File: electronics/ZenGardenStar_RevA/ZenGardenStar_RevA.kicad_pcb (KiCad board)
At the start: 2 copper layers, 13 parts, among them P1 CONN_01X02, P2 CONN_01X02, U1 A6211, U2 LM317_SOT223, U3 ArduinoProMini328, U4 MCP1700, U5 NRF24L01+

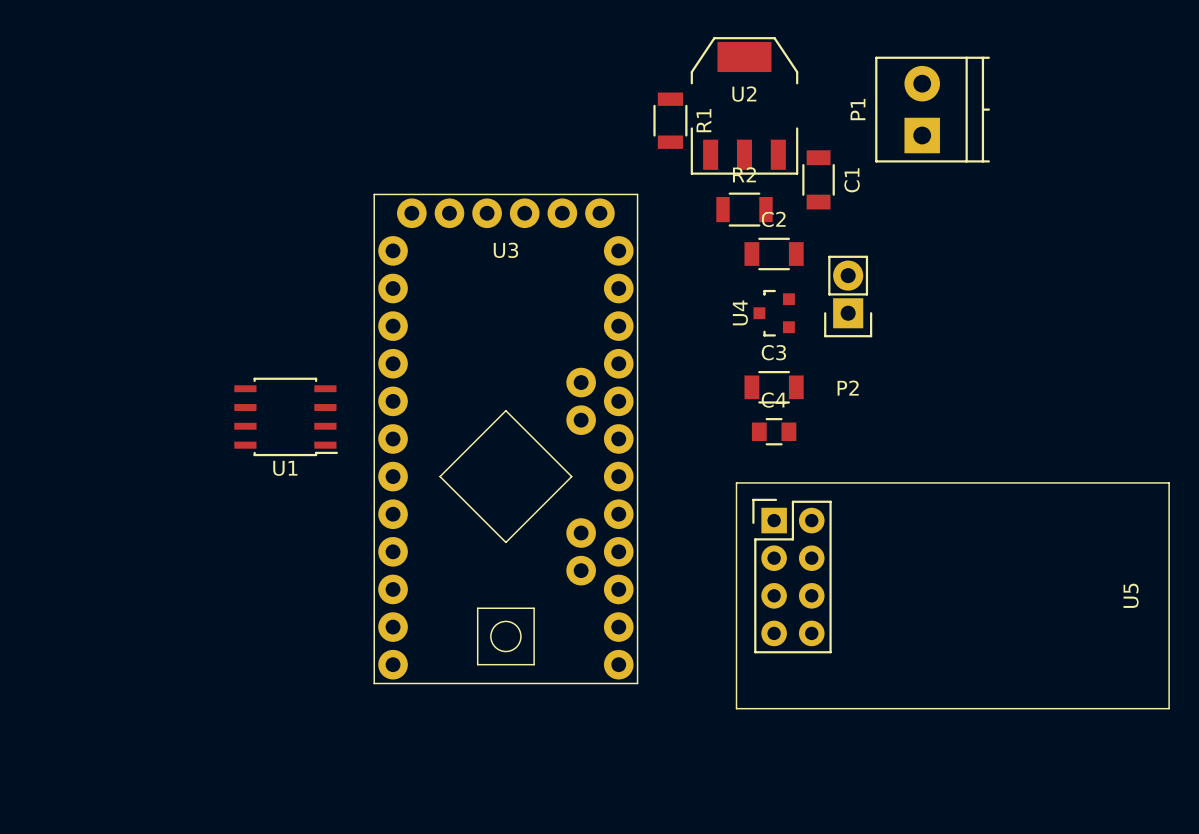
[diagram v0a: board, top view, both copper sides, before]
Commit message: updated schematic for star
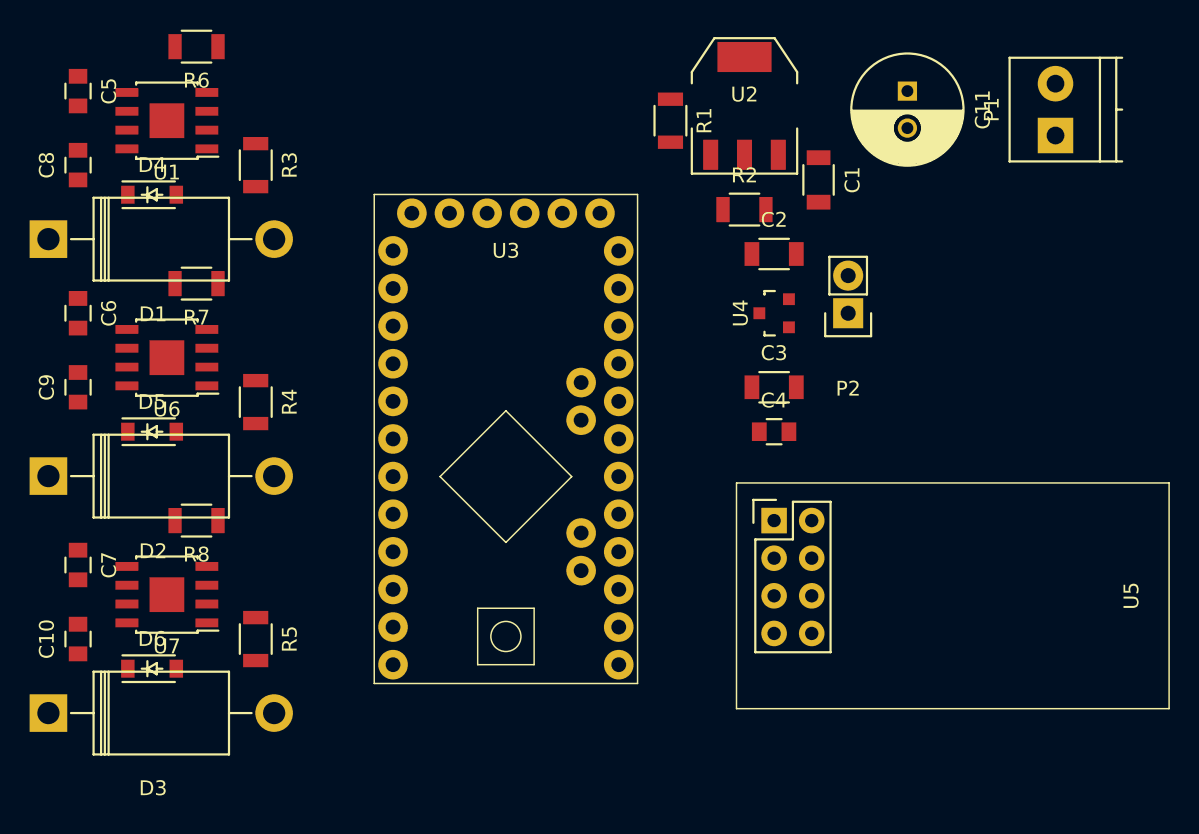
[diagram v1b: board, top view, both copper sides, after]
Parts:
- added C10: 0.047uF 50V, Capacitors_SMD:C_0805, F.Cu at (113.0, 108.0)
- added C11: 47uF 50V, Capacitors_ThroughHole:C_Radial_D7.5_L11.2_P2.5, F.Cu at (169.0, 71.0)
- added C5: 0.1uF 10V, Capacitors_SMD:C_0805, F.Cu at (113.0, 71.0)
- added C6: 0.1uF 10V, Capacitors_SMD:C_0805, F.Cu at (113.0, 86.0)
- added C7: 0.1uF 10V, Capacitors_SMD:C_0805, F.Cu at (113.0, 103.0)
- added C8: 0.047uF 50V, Capacitors_SMD:C_0805, F.Cu at (113.0, 76.0)
- added C9: 0.047uF 50V, Capacitors_SMD:C_0805, F.Cu at (113.0, 91.0)
- added D1: 60V 3A SR306, Diodes_ThroughHole:Diode_DO-201AD_Horizontal_RM15, F.Cu at (111.0, 81.0)
- added D2: 60V 3A SR306, Diodes_ThroughHole:Diode_DO-201AD_Horizontal_RM15, F.Cu at (111.0, 97.0)
- added D3: 60V 3A SR306, Diodes_ThroughHole:Diode_DO-201AD_Horizontal_RM15, F.Cu at (111.0, 113.0)
- added D4: 60V 3A PMEG6030EP, Diodes_SMD:SOD-123, F.Cu at (118.0, 78.0)
- added D5: 60V 3A PMEG6030EP, Diodes_SMD:SOD-123, F.Cu at (118.0, 94.0)
- added D6: 60V 3A PMEG6030EP, Diodes_SMD:SOD-123, F.Cu at (118.0, 110.0)
- added R3: 72K, Resistors_SMD:R_1206, F.Cu at (125.0, 76.0)
- added R4: 72K, Resistors_SMD:R_1206, F.Cu at (125.0, 92.0)
- added R5: 72K, Resistors_SMD:R_1206, F.Cu at (125.0, 108.0)
- added R6: 0.43, Resistors_SMD:R_1206, F.Cu at (121.0, 68.0)
- added R7: 0.43, Resistors_SMD:R_1206, F.Cu at (121.0, 84.0)
- added R8: 0.43, Resistors_SMD:R_1206, F.Cu at (121.0, 100.0)
- added U6: A6211, Housings_SOIC:SOIC-8-1EP_3.9x4.9mm_Pitch1.27mm, F.Cu at (119.0, 89.0)
- added U7: A6211, Housings_SOIC:SOIC-8-1EP_3.9x4.9mm_Pitch1.27mm, F.Cu at (119.0, 105.0)
- C1: value 10uF -> 10uF 50V
- C2: value 10uF -> 10uF 10V
- U1: footprint MyKiCadParts:SOIC-8-N-80 -> Housings_SOIC:SOIC-8-1EP_3.9x4.9mm_Pitch1.27mm
- moved U1 21.5 mm to (119.0, 73.0)
- moved P1 9.00 mm to (179.0, 74.0)
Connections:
- U1 pad 2: (no net) -> Net-(R3-Pad1)
- U1 pad 4: (no net) -> Net-(R6-Pad1)
- U1 pad 5: V50 -> Net-(C5-Pad1)
- U1 pad 7: (no net) -> Net-(C8-Pad2)
- U1 pad 8: (no net) -> Net-(C8-Pad1)
- U3 pad 8: (no net) -> PWM_G
- U3 pad 9: (no net) -> PWM_B

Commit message: updated star layout and schematic and render, at 80-90% done
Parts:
- added L1: INDUCTOR_SMALL, Inductors:SELF-WE-PD-XXL, F.Cu at (104.0, 73.0)
- added L2: INDUCTOR_SMALL, Inductors:SELF-WE-PD-XXL, F.Cu at (104.0, 89.0)
- added L3: INDUCTOR_SMALL, Inductors:SELF-WE-PD-XXL, F.Cu at (104.0, 105.0)
- added P3: CONN_PIR_0, Pin_Headers:Pin_Header_Straight_1x03, F.Cu at (135.0, 110.0)
- added P4: CONN_PIR_1, Pin_Headers:Pin_Header_Straight_1x03, F.Cu at (142.0, 110.0)
- added P5: CONN_R, Pin_Headers:Pin_Header_Straight_1x02, F.Cu at (105.0, 65.0)
- added P6: CONN_B, Pin_Headers:Pin_Header_Straight_1x02, F.Cu at (105.0, 97.0)
- added P7: CONN_G, Pin_Headers:Pin_Header_Straight_1x02, F.Cu at (105.0, 81.0)
- P2: value CONN_01X02 -> CONN_VDD
- moved C11 17.5 mm to (152.0, 67.0)
- moved P1 16.8 mm to (163.0, 69.0)
- moved U3 5.83 mm to (130.0, 106.0)
- moved C1 4.00 mm to (163.0, 81.0)
- moved C2 4.00 mm to (160.0, 86.0)
- moved C3 4.00 mm to (160.0, 95.0)
- moved C4 4.00 mm to (160.0, 98.0)
- moved P2 4.00 mm to (165.0, 90.0)
- moved R1 4.00 mm to (153.0, 77.0)
- moved R2 4.00 mm to (158.0, 83.0)
- moved U2 4.00 mm to (158.0, 76.0)
- moved U4 4.00 mm to (160.0, 90.0)
- moved U5 4.00 mm to (160.0, 104.0)
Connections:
- U3 pad 10: (no net) -> PIR_0
- U3 pad 11: (no net) -> PIR_1
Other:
- board outline added: 75 x 60 mm

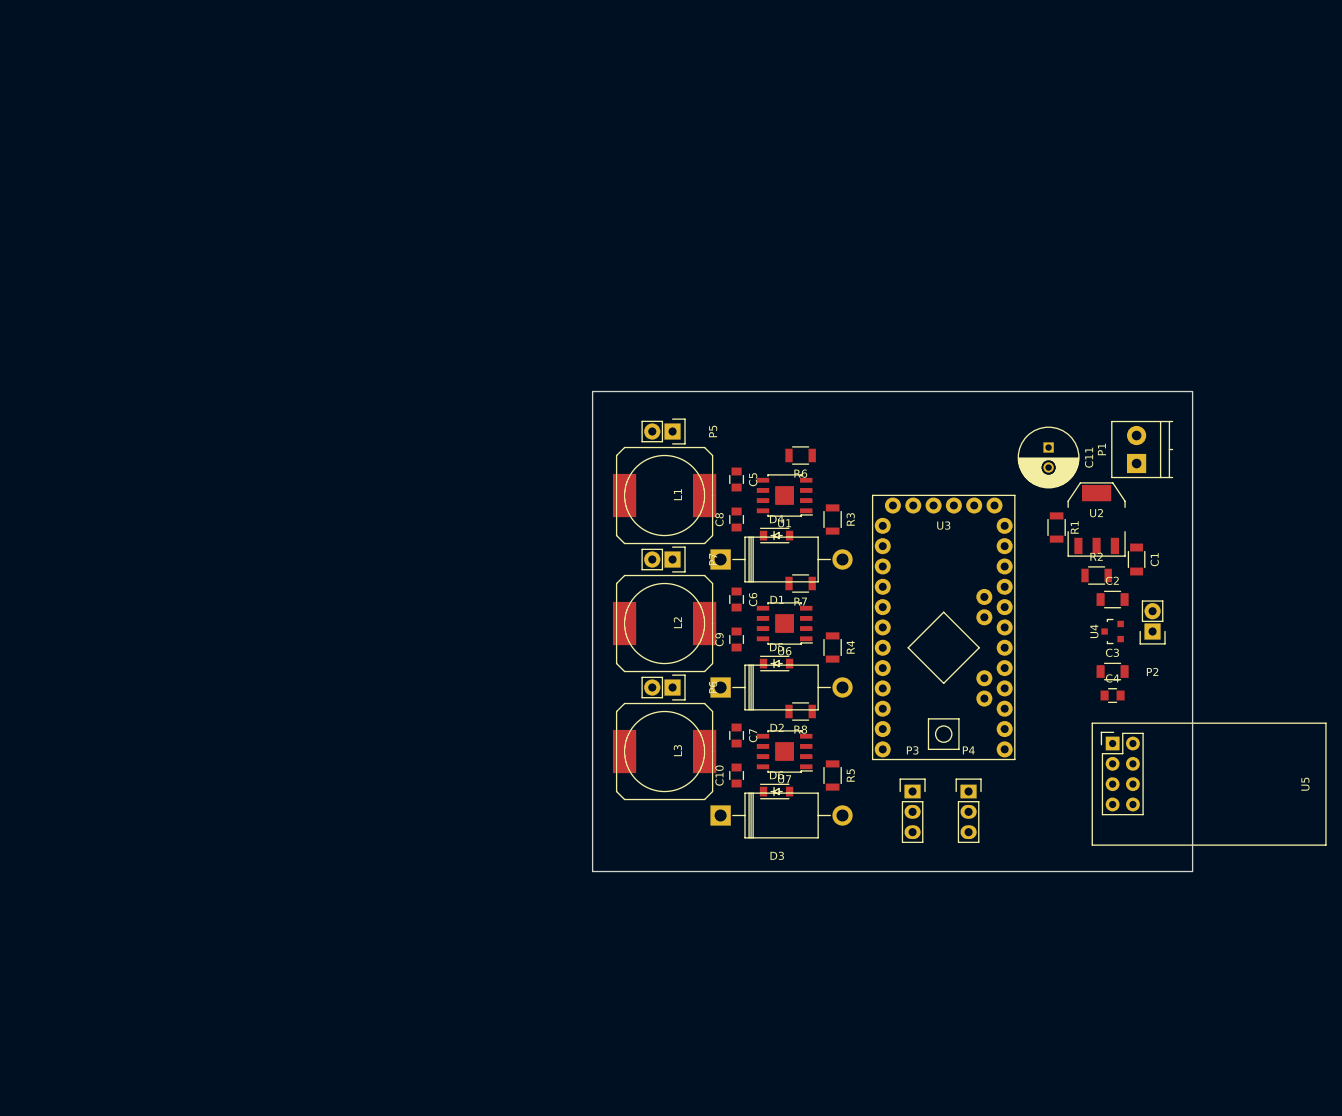
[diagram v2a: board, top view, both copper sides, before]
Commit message: some updates to the star schematics and layout; schematic pretty much final
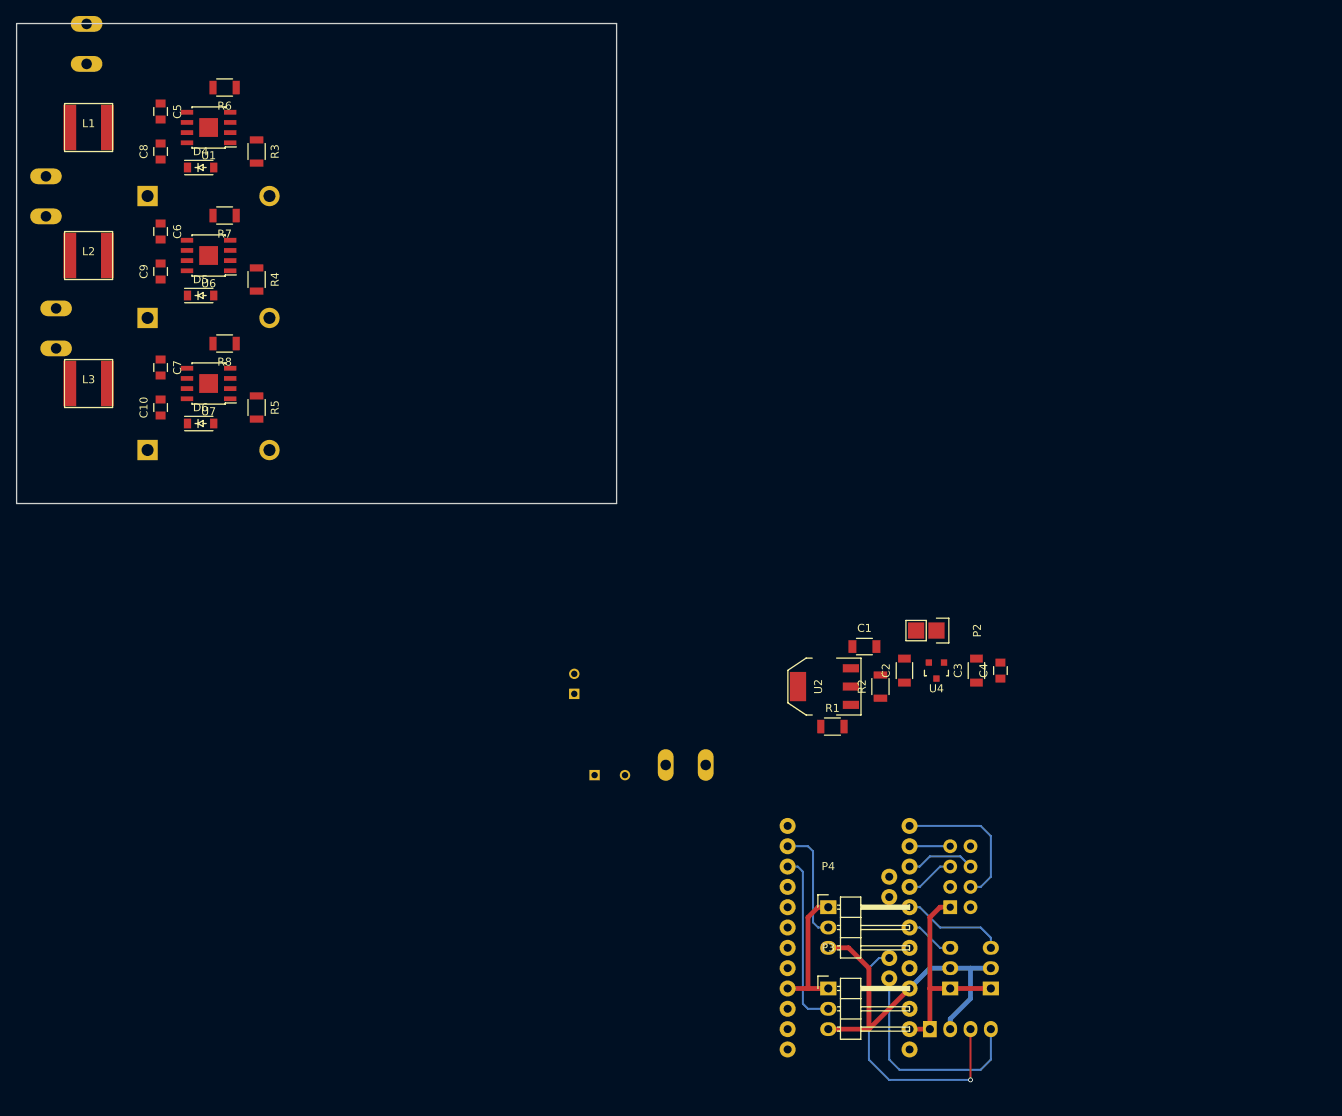
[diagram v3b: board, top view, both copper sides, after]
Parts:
- added C12: 100uF 50V, Capacitors_ThroughHole:C_Radial_D8_L13_P3.8, B.Cu at (95.2, 108.0)
- added P10: CONN_I2C, Pin_Headers:Pin_Header_Straight_1x04, B.Cu at (137.2, 139.7)
- added P8: CONN_A0, Pin_Headers:Pin_Header_Straight_1x03, B.Cu at (144.8, 134.6)
- added P9: CONN_A1, Pin_Headers:Pin_Header_Straight_1x03, B.Cu at (139.7, 134.6)
- C11, D1, D2, D3, U3, U5: moved to B.Cu
- L1, L2, L3: value INDUCTOR_SMALL -> 47uH 1A; footprint Inductors:SELF-WE-PD-XXL -> MyKiCadParts:TAIYO_YUDEN_IND_6045
- P1: footprint Terminal_Blocks:TerminalBlock_Pheonix_PT-3.5mm_2pol -> Connect:AK300-2; moved to B.Cu
- P3, P4: footprint Pin_Headers:Pin_Header_Straight_1x03 -> Pin_Headers:Pin_Header_Angled_1x03
- P5, P6, P7: footprint Pin_Headers:Pin_Header_Straight_1x02 -> Connect:AK300-2; moved to B.Cu
- moved P7 89.3 mm to (26.7, 38.1), turned to 90 degrees
- moved P6 87.9 mm to (27.9, 54.6), turned to 90 degrees
- moved P5 86.5 mm to (31.8, 19.1), turned to 90 degrees
- moved C10 85.4 mm to (41.0, 62.0)
- moved C5 85.4 mm to (41.0, 25.0)
- moved C6 85.4 mm to (41.0, 40.0)
- moved C7 85.4 mm to (41.0, 57.0)
- moved C8 85.4 mm to (41.0, 30.0)
- moved C9 85.4 mm to (41.0, 45.0)
- moved D4 85.4 mm to (46.0, 32.0)
- moved D5 85.4 mm to (46.0, 48.0)
- moved D6 85.4 mm to (46.0, 64.0)
- moved L1 85.4 mm to (32.0, 27.0)
- moved L2 85.4 mm to (32.0, 43.0)
- moved L3 85.4 mm to (32.0, 59.0)
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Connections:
- U3 pad 17: (no net) -> A0
- U3 pad 18: (no net) -> A1
- U3 pad 31: (no net) -> SCL
- U3 pad 32: (no net) -> SDA
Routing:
- net V50: track 0.00 -> 45.9 mm
- net GND: track 0.00 -> 44.2 mm
- net SDA: track 0.00 -> 34.6 mm, vias 0 -> 1
- net SCL: track 0.00 -> 27.7 mm
- net PIR_0: track 0.00 -> 22.1 mm
- net CSN: track 0.00 -> 18.8 mm
- net PIR_1: track 0.00 -> 14.5 mm
- net A0: track 0.00 -> 13.0 mm
- net MISO: track 0.00 -> 8.67 mm
- net SCK: track 0.00 -> 6.13 mm
- net A1: track 0.00 -> 6.13 mm
- net MOSI: track 0.00 -> 5.08 mm
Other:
- net class Default: clearance 0.8 -> 0.2; trace_width 0.3 -> 0.25
- rule trace_clearance: 0.8 -> 0.2

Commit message: near final pcb layout
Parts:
- added REF**: MountingHole_3mm, Mounting_Holes:MountingHole_3mm, F.Cu at (120.0, 104.8)
- added REF**: MountingHole_3mm, Mounting_Holes:MountingHole_3mm, F.Cu at (144.8, 144.8)
- added REF**: MountingHole_3mm, Mounting_Holes:MountingHole_3mm, F.Cu at (124.5, 143.5)
- added REF**: MountingHole_3mm, Mounting_Holes:MountingHole_3mm, F.Cu at (143.5, 102.9)
- C1: value 10uF 50V -> 10uF50V
- P2: moved to B.Cu
- P3, P4: footprint Pin_Headers:Pin_Header_Angled_1x03 -> Pin_Headers:Pin_Header_Straight_1x03; moved to B.Cu
- moved P5 138.5 mm to (104.1, 137.2)
- moved L1 136.5 mm to (105.2, 142.2)
- moved D1 133.0 mm to (115.3, 144.8), turned to 120 degrees
- moved C8 131.9 mm to (110.2, 142.2), turned to 0 degrees
- moved R6 130.2 mm to (114.3, 134.6)
- moved D4 129.6 mm to (110.7, 144.3)
- moved C5 129.4 mm to (109.7, 134.6), turned to 0 degrees
- moved U1 129.4 mm to (112.3, 138.7)
- moved R3 128.1 mm to (114.8, 142.2), turned to 180 degrees
- moved P7 114.1 mm to (104.1, 121.9)
- moved L2 111.4 mm to (105.2, 127.0)
- moved D2 109.0 mm to (114.8, 129.5), turned to 120 degrees
- moved C9 107.3 mm to (110.2, 127.0), turned to 0 degrees
- moved C6 105.0 mm to (109.7, 119.4), turned to 0 degrees
- moved R7 104.3 mm to (114.3, 119.4)
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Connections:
- P5 pad 1: Net-(P5-Pad1) -> Net-(L1-Pad2)
- P5 pad 2: Net-(L1-Pad2) -> Net-(P5-Pad2)
- P6 pad 1: Net-(P6-Pad1) -> Net-(L3-Pad2)
- P6 pad 2: Net-(L3-Pad2) -> Net-(P6-Pad2)
- P7 pad 1: Net-(P7-Pad1) -> Net-(L2-Pad2)
- P7 pad 2: Net-(L2-Pad2) -> Net-(P7-Pad2)
- R6 pad 1: Net-(P5-Pad1) -> Net-(P5-Pad2)
- R7 pad 1: Net-(P7-Pad1) -> Net-(P7-Pad2)
- R8 pad 1: Net-(P6-Pad1) -> Net-(P6-Pad2)
- U1 pad 4: Net-(P5-Pad1) -> Net-(P5-Pad2)
- U3 pad 1: (no net) -> Net-(U3-Pad1)
- U3 pad 10: PIR_0 -> Net-(U3-Pad10)
- U3 pad 11: PIR_1 -> Net-(U3-Pad11)
- U3 pad 19: (no net) -> PIR_0
- U3 pad 2: (no net) -> Net-(U3-Pad2)
- U3 pad 20: (no net) -> PIR_1
- U3 pad 22: (no net) -> Net-(U3-Pad22)
- U3 pad 24: (no net) -> Net-(U3-Pad24)
- U3 pad 3: (no net) -> Net-(U3-Pad3)
- U3 pad 33: (no net) -> Net-(U3-Pad33)
- U3 pad 34: (no net) -> Net-(U3-Pad34)
- U3 pad 5: (no net) -> Net-(U3-Pad5)
- U3 pad 7: (no net) -> Net-(U3-Pad7)
- U5 pad 8: (no net) -> Net-(U5-Pad8)
- U6 pad 4: Net-(P7-Pad1) -> Net-(P7-Pad2)
- U7 pad 4: Net-(P6-Pad1) -> Net-(P6-Pad2)
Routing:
- net GND: track 44.2 -> 212.3 mm
- net V36: track 0.00 -> 80.3 mm, vias 0 -> 3
- net CE: track 0.00 -> 29.4 mm, vias 0 -> 1
- net V33: track 0.00 -> 27.2 mm, vias 0 -> 3
- net V50: track 45.9 -> 73.0 mm, vias 0 -> 3
- net PWM_B: track 0.00 -> 17.5 mm
- net Net-(P7-Pad2): track 0.00 -> 15.8 mm, vias 0 -> 1
- net Net-(P5-Pad2): track 0.00 -> 15.8 mm, vias 0 -> 1
- net Net-(P6-Pad2): track 0.00 -> 15.8 mm, vias 0 -> 1
- net Net-(C8-Pad1): track 0.00 -> 12.0 mm, vias 0 -> 1
- net PWM_R: track 0.00 -> 11.8 mm
- net Net-(C9-Pad1): track 0.00 -> 11.7 mm, vias 0 -> 1
- net PIR_0: track 22.1 -> 10.5 mm
- net Net-(C10-Pad1): track 0.00 -> 11.5 mm, vias 0 -> 1
- net SDA: track 34.6 -> 26.3 mm
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- added copper zone on B.Cu, net GND
- added copper zone on F.Cu, net GND
- added copper zone on B.Cu, net V36
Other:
- board size 75 x 60 mm -> 48.3 x 48.3 mm
- board text added: "Bridge if V50 = V33"
- board text added: "GND PIR0 V50"
- board text added: "GND PIR1 V50"
- board text added: "GND V50 A0"
- board text added: "GND V50 A1"
- board text added: "GND V50 SDA SCL"

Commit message: final pcb layout ready, gerbers created, order prepared
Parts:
- moved REF** 1.91 mm to (120.0, 102.9)
- moved REF** 1.80 mm to (143.5, 143.5)
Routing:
- net GND: track 212.3 -> 213.4 mm
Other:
- board text added: "+B+ -B-"
- board text added: "+G+ -G-"
- board text added: "+R+ -R-"
- board text added: "GND 36V"
- board text added: "Matthew Swarts 2017.03.13"
- board text added: "Zen Garden Star Rev A"
